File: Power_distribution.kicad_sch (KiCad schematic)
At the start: 30 parts, among them J24 Conn_01x02, U10 MP2491C, U11 AMS1117-3.3, U14 MIC2026-1xM, U15 MIC2026-1xM, U17 MIC2026-1xM, U9 MP2491C

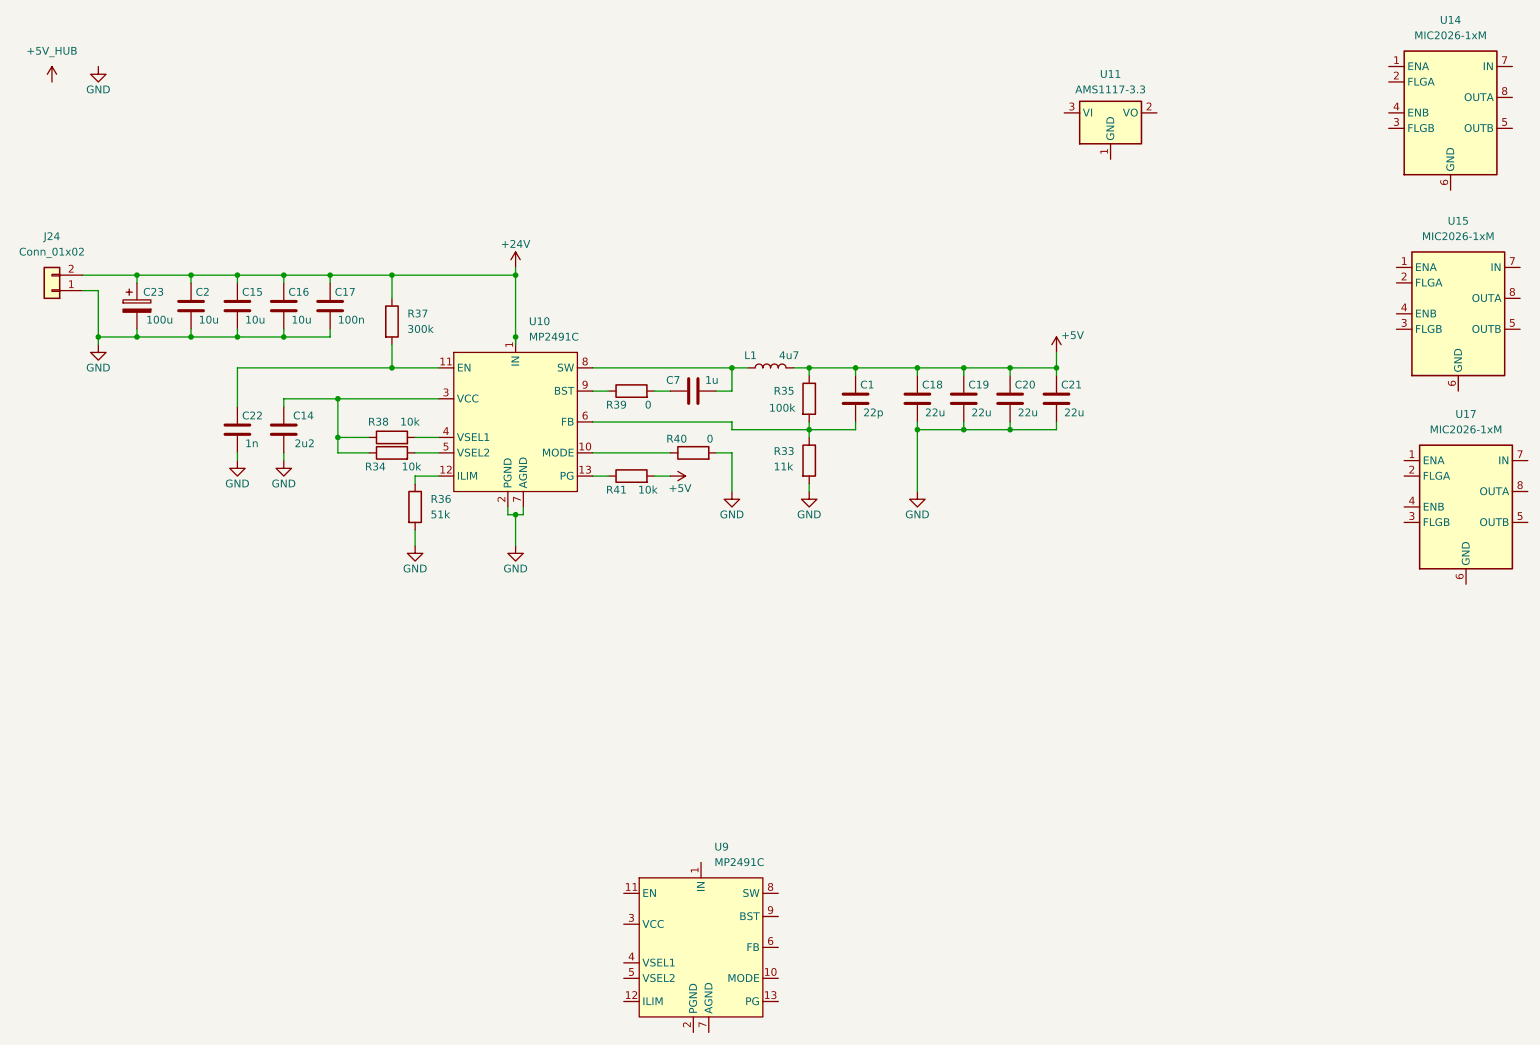
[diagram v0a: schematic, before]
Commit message: Changes in schematic to fit DC/DC converter
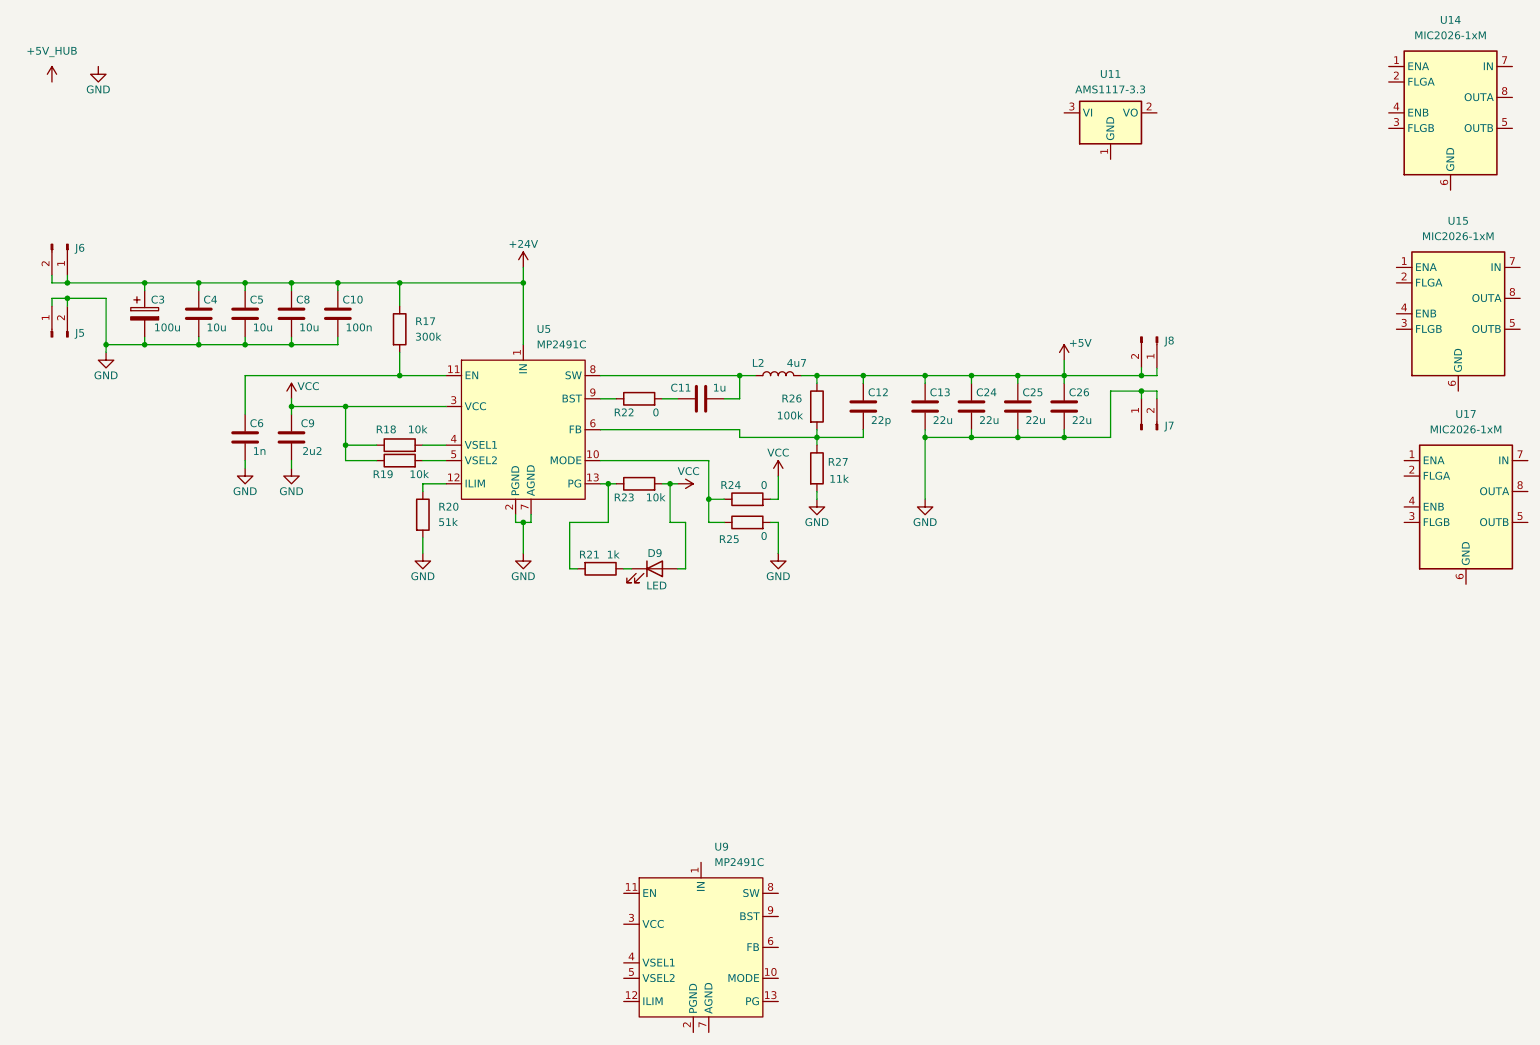
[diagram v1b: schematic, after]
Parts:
- removed C1: 22p, symbol Device:C
- removed C14: 2u2, symbol Device:C
- removed C15, C16, C2: 10u, symbol Device:C
- removed C17: 100n, symbol Device:C
- removed C18, C19, C20, C21: 22u, symbol Device:C
- removed C22: 1n, symbol Device:C
- removed C23: 100u, symbol Device:C_Polarized
- removed C7: 1u, symbol Device:C
- removed J24: Conn_01x02, Connector_Phoenix_MSTB:PhoenixContact_MSTBA_2,5_2-G_1x02_P5.00mm_Horizontal, symbol Connector_Generic:Conn_01x02
- removed L1: 4u7, symbol Device:L
- removed R33: 11k, symbol Device:R
- removed R34, R38, R41: 10k, symbol Device:R
- removed R35: 100k, symbol Device:R
- removed R36: 51k, symbol Device:R
- removed R37: 300k, symbol Device:R
- removed R39, R40: 0, symbol Device:R
- removed U10: MP2491C, HK:QFN-13_HK, symbol HK:MP2491C_HK
- added C10: 100n, Capacitor_SMD:C_0603_1608Metric, symbol Device:C
- added C11: 1u, Capacitor_SMD:C_0603_1608Metric, symbol Device:C
- added C12: 22p, Capacitor_SMD:C_0603_1608Metric, symbol Device:C
- added C13, C24, C25, C26: 22u, Capacitor_SMD:C_0805_2012Metric, symbol Device:C
- added C3: 100u, Capacitor_THT:CP_Radial_D6.3mm_P2.50mm, symbol Device:C_Polarized
- added C4, C5, C8: 10u, Capacitor_SMD:C_0805_2012Metric, symbol Device:C
- added C6: 1n, Capacitor_SMD:C_0603_1608Metric, symbol Device:C
- added C9: 2u2, Capacitor_SMD:C_0603_1608Metric, symbol Device:C
- added D9: LED, LED_SMD:LED_0603_1608Metric, symbol Device:LED
- added J5, J6, J7, J8: Conn_01x02_Pin, Connector_PinHeader_2.54mm:PinHeader_1x02_P2.54mm_Vertical, symbol Connector:Conn_01x02_Pin
- added L2: 4u7, HK:Inductor_IHLP3232DZER4R7M11_HK, symbol Device:L
- added R17: 300k, Resistor_SMD:R_0603_1608Metric, symbol Device:R
- added R18, R19, R23: 10k, Resistor_SMD:R_0603_1608Metric, symbol Device:R
- added R20: 51k, Resistor_SMD:R_0603_1608Metric, symbol Device:R
- added R21: 1k, Resistor_SMD:R_0603_1608Metric, symbol Device:R
- added R22, R24, R25: 0, Resistor_SMD:R_0603_1608Metric, symbol Device:R
- added R26: 100k, Resistor_SMD:R_0603_1608Metric, symbol Device:R
- added R27: 11k, Resistor_SMD:R_0603_1608Metric, symbol Device:R
- added U5: MP2491C, HK:QFN-13_HK, symbol HK:MP2491C_HK
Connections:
- net +24V: now also C10.1, C3.1, C4.1, C5.1, C8.1, J6.1 (Pin_1), J6.2 (Pin_2), R17.1, U5.1 (IN)
- net +5V: now also C12.1, C13.1, C24.1, C25.1, C26.1, J8.1 (Pin_1), J8.2 (Pin_2), L2.2, R26.1
- net GND: now also C10.2, C13.2, C24.2, C25.2, C26.2, C3.2, C4.2, C5.2, C6.2, C8.2, C9.2, J5.1 (Pin_1), J5.2 (Pin_2), J7.1 (Pin_1), J7.2 (Pin_2), R20.2, R25.2, R27.2, U5.2 (PGND), U5.7 (AGND)
- new net: C6.1, R17.2, U5.11 (EN)
- new net: D9.1 (K), R21.1
- new net: C12.2, R26.2, R27.1, U5.6 (FB)
- new net: R22.1, U5.9 (BST)
- new net: C11.2, R22.2
- new net: R18.2, U5.4 (VSEL1)
- new net: R19.2, U5.5 (VSEL2)
- new net: R24.1, R25.1, U5.10 (MODE)
- new net: R20.1, U5.12 (ILIM)
- new net: R21.2, R23.1, U5.13 (PG)
- new net: C11.1, L2.1, U5.8 (SW)
- new net VCC: C9.1, D9.2 (A), R18.1, R19.1, R23.2, R24.2, U5.3 (VCC)

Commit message: PCB rebuilt
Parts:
- removed J5, J6, J7, J8: Conn_01x02_Pin, Connector_PinHeader_2.54mm:PinHeader_1x02_P2.54mm_Vertical, symbol Connector:Conn_01x02_Pin
- removed U11: AMS1117-3.3, Package_TO_SOT_SMD:SOT-223-3_TabPin2, symbol Regulator_Linear:AMS1117-3.3
- removed U14, U15, U17: MIC2026-1xM, Package_SO:SOIC-8_3.9x4.9mm_P1.27mm, symbol Power_Management:MIC2026-1xM
- removed U9: MP2491C, HK:QFN-13_HK, symbol HK:MP2491C_HK
- added J11: PWR_input, Connector_Phoenix_MSTB:PhoenixContact_MSTBA_2,5_2-G_1x02_P5.00mm_Horizontal, symbol Connector:Screw_Terminal_01x02
- renumbered C3 to C1, C6 to C10, C9 to C11, C11 to C12, C12 to C13, C4 to C2, C5 to C3, C8 to C4, C10 to C5, C13 to C6, C24 to C7, C25 to C8, C26 to C9, D9 to D26, L2 to L1, R17 to R58, R18 to R59, R19 to R60, R20 to R61, R21 to R62, R22 to R63, R23 to R64, R24 to R65, R25 to R66, R26 to R67, R27 to R68, U5 to U1
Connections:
- net +24V: now also J11.2 (Pin_2)
- net GND: now also J11.1 (Pin_1)
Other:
- moved on the sheet: C1, C10, C11, C12, C13, C2, C3, C4, C5, C6, C7, C8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

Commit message: Made the PCK the size of the LP board
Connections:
- net +24V: now also J11.1 (Pin_1); no longer J11.2 (Pin_2)
- net GND: now also J11.2 (Pin_2); no longer J11.1 (Pin_1)
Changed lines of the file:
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@@
 	(symbol
 		(lib_id "Connector:Screw_Terminal_01x02")
-		(at 99.06 43.18 0)
-		(mirror x)
+		(at 99.06 40.64 0)
 		(unit 1)
 		(exclude_from_sim no)
@@
 		(dnp no)
 		(property "Reference" "J11"
-			(at 101.6 43.1801 0)
+			(at 101.6 40.6399 0)
 			(effects
 				(font
@@
 		)
 		(property "Value" "PWR_input"
-			(at 101.6 40.6401 0)
+			(at 101.6 43.1799 0)
 			(effects
 				(font
@@
 		)
 		(property "Footprint" "Connector_Phoenix_MSTB:PhoenixContact_MSTBA_2,5_2-G_1x02_P5.00mm_Horizontal"
-			(at 99.06 43.18 0)
+			(at 99.06 40.64 0)
 			(effects
 				(font
@@
 		)
 		(property "Datasheet" "~"
-			(at 99.06 43.18 0)
+			(at 99.06 40.64 0)
 			(effects
 				(font
@@
 		)
 		(property "Description" "Generic screw terminal, single row, 01x02, script generated (kicad-library-utils/schlib/autogen/connector/)"
-			(at 99.06 43.18 0)
+			(at 99.06 40.64 0)
 			(effects
 				(font
